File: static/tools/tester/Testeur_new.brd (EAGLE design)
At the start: 101.6 x 108 mm, 30 parts, among them IC1 MEGA8-P

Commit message: [tester] modify to V2 Alpha.
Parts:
- removed CODER-MOTOR, I²C, SV1: (no value), con-lstb:MA04-1
- removed ENCODER-SELECT, LCD-GND: (no value), con-lstb:MA05-1
- removed LCD-CONTRASTE, POTAR-CONTRASTE, RETURN, SERVO/PWM: (no value), con-lstb:MA03-1
- removed LCD-DATA: (no value), con-lstb:MA06-1
- removed LCD1-IHM, LCD2-IHM: (no value), con-lstb:MA08-1
- added AR, RETURN_IHM: (no value), pinhead:1X02
- added C1-REGULATOR1, C2-REGULATOR1: (no value), capacitor-wima:C5B5
- added IC3: (no value), v-reg:78XXS
- added JP1, JP2: (no value), pinhead:2X12
- added JP3: (no value), pinhead:1X16
- added MOTOR, X1: (no value), con-wago-500:W237-102
- added POTAR, SERVO-IHM2: (no value), con-lstb:MA03-1
- added Q2: MFR475V, transistor-power:TO220AV
- added R2: (no value), resistor:0204/7
- ALIM: device con-lstb:MA03-1 -> pinhead:1X02
- LED1, LED2: device led:LED3MM -> led:LED5MM
- R1: device rcl:0204/5 -> rcl:0204/7
- moved LED1 72.8 mm to (-3.81, -50.2), turned to 180 degrees
- moved LED2 71.8 mm to (-3.81, -43.8), turned to 180 degrees
- moved ALIM 34.4 mm to (1.91, 15.2), turned to 270 degrees
- moved IC2 27.4 mm to (-4.45, 16.5), turned to 90 degrees
- moved C1-REGULATOR 24.8 mm to (-0.64, 8.89), turned to 0 degrees
- moved C2-REGULATOR 22.8 mm to (-0.64, 24.1), turned to 0 degrees
- moved CODER-IHM 14.6 mm to (26.0, -17.8), turned to 90 degrees
- moved SERVO-IHM 14.2 mm to (44.5, -19.1), turned to 90 degrees
- moved IC1 9.44 mm to (26.0, 25.4)
- moved R3 8.64 mm to (38.1, 15.2), turned to 270 degrees
- moved R4 8.64 mm to (34.9, 15.2), turned to 270 degrees
- moved C1-CRYSTAL 8.13 mm to (26.0, 37.5), turned to 90 degrees
- moved C2-CRYSTAL 8.13 mm to (15.9, 37.5), turned to 270 degrees
- moved Q1 8.13 mm to (21.0, 37.5), turned to 270 degrees
- moved UART-IHM 6.98 mm to (15.9, -17.8), turned to 90 degrees
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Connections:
- net N$25 renamed LED1
- net N$26 renamed LED2
- removed net N$5: CODER-MOTOR.2, IC1.5
- new net 5V_POWER: C2-REGULATOR1.1, IC3.OUT, SERVO-IHM.2, SERVO-IHM2.2
- new net 5V_POW_IHM: JP2.3
- new net ALIM_EXT: C1-REGULATOR1.1, IC3.IN, MOTOR.1, X1.1
- new net ENCODER1: IC1.6, JP1.24
- new net ENCODER2: IC1.11, JP1.23
- new net GND_IHM: AR.1, C1-REGULATOR1.2, C2-REGULATOR1.2, CODER-IHM.2, ENCODER-IHM.C, ENCODER-IHM.D, I2C-IHM.2, IC3.GND, JP2.1, JP3.1, JP3.10, JP3.5, JP3.7, JP3.8, JP3.9, LED1.K, LED2.K, POTAR.3, Q2.E, RETURN_IHM.1, SERVO-IHM.1, SERVO-IHM2.1, UART-IHM.2, X1.2
- new net INT_ODO1: IC1.4, JP1.18
- new net LCD1: IC1.13, JP1.19
- new net LCD2: IC1.14, JP1.17
- new net LCD3: IC1.15, JP1.15
- new net LCD5: IC1.18, JP1.9
- new net LCD6: IC1.19, JP1.7
- new net N$25: JP2.19, JP3.4
- new net N$26: JP2.17, JP3.6
- new net N$34: JP2.7, JP3.14
- new net N$35: JP2.11, R2.1, SERVO-IHM.3
- new net N$36: JP2.8, RETURN_IHM.2
- new net N$37: AR.2, JP2.2
- new net N$39: JP3.3, POTAR.1
- new net N$40: MOTOR.2, Q2.C
- new net RETURN: IC1.26, JP1.8
- new net RX: IC1.2, JP1.14
- new net SCL: IC1.28, JP1.12
- new net SDA: IC1.27, JP1.10
- new net SELECT: IC1.12, JP1.21
- new net SENS_ODO+SERVO2: IC1.5, JP1.22
- new net SERVO/PWM: IC1.17, JP1.11
- new net TX: IC1.3, JP1.16
- new net VCC_IHM: CODER-IHM.1, I2C-IHM.1, JP2.5, JP3.2, POTAR.2, UART-IHM.1
- net GND: now also JP1.1; no longer CODER-MOTOR.4, ENCODER-SELECT.4, ENCODER-SELECT.5, I²C.2, LCD-CONTRASTE.3, LCD-GND.1, LCD-GND.2, LCD-GND.3, LCD-GND.4, LCD-GND.5, LED1.K, LED2.K, POTAR-CONTRASTE.3, RETURN.3, SERVO/PWM.3, SV1.3
- net N$10: now also I2C-IHM.3, JP2.10; no longer IC1.14, LCD-DATA.2
- net N$11: now also I2C-IHM.4, JP2.12; no longer IC1.17, SERVO/PWM.1
- net N$12: now also JP2.4, LED1.A; no longer IC1.19, LCD-DATA.6
- net N$13: now also JP2.6, LED2.A; no longer IC1.13, LCD-DATA.1
- net N$14: now also JP2.14, UART-IHM.3; no longer IC1.15, LCD-DATA.3
- net N$15: now also JP2.16, UART-IHM.4; no longer IC1.16, LCD-DATA.4
- net N$16: now also CODER-IHM.3, JP2.18; no longer IC1.18, LCD-DATA.5
- net N$17: now also CODER-IHM.4, JP2.22, SERVO-IHM2.3; no longer CODER-MOTOR.1, IC1.4
- net N$18: now also ENCODER-IHM.A, JP2.24; no longer LED2.A, R3.2
- net N$21: now also ENCODER-IHM.B, JP2.23; no longer IC1.2, SV1.1
- net N$22: now also ENCODER-IHM.E, JP2.21; no longer IC1.3, SV1.2
- net N$27: now also JP2.15, JP3.11; no longer IC1.26, RETURN.1
- net N$28: now also JP1.4; no longer LED1.A
- net N$29: now also JP2.13, JP3.12; no longer IC1.27, I²C.3
- net N$3: now also IC1.23, JP1.2; no longer LCD-CONTRASTE.1, POTAR-CONTRASTE.1
- net N$30: now also JP2.9, JP3.13; no longer IC1.28, I²C.4
- net N$6: now also ALIM.2; no longer ALIM.3
- net N$7: now also JP1.6, R3.2; no longer ENCODER-SELECT.1, IC1.6
- net N$8: now also Q2.B, R2.2; no longer ENCODER-SELECT.2, IC1.11
- net N$9: now also IC1.16, JP1.13; no longer ENCODER-SELECT.3, IC1.12
- net VCC: now also JP1.5; no longer CODER-MOTOR.3, I²C.1, LCD-CONTRASTE.2, POTAR-CONTRASTE.2, SERVO/PWM.2, SV1.4
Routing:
- net GND_IHM: track 0.00 -> 249.3 mm
- net GND: track 229.5 -> 90.8 mm, vias 2 -> 0
- net N$17: track 7.62 -> 111.0 mm
- net ENCODER1: track 0.00 -> 99.1 mm
- net VCC: track 160.4 -> 69.0 mm, vias 6 -> 0
- net SENS_ODO+SERVO2: track 0.00 -> 90.3 mm, vias 0 -> 1
- net N$21: track 9.04 -> 91.7 mm
- net ALIM_EXT: track 0.00 -> 72.6 mm
- net INT_ODO1: track 0.00 -> 71.6 mm
- net N$15: track 15.3 -> 82.8 mm
- net N$22: track 13.0 -> 77.5 mm
- net N$10: track 8.89 -> 73.0 mm
- net VCC_IHM: track 0.00 -> 64.0 mm, vias 0 -> 1
- net N$14: track 11.7 -> 75.2 mm
- net N$18: track 12.5 -> 73.7 mm
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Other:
- board text added: "A"
- board text added: "AR"
- board text added: "B"
- board text added: "GND"
- board text added: "I²C"
- board text added: "LED1"
- board text added: "LED2"
- board text added: "MOTOR"
- board text added: "POWER"
- board text added: "UART"
- board text added: "codeur"
- board text added: "encoder"
- board text added: "potar"
- board text added: "return"
- board text added: "servo"
- board text added: "servo2"

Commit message: [tester] improve V2.
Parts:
- removed UART-IHM: (no value), con-lstb:MA04-1
- added SERVO-IHM1: (no value), con-lstb:MA03-1
- added SWITCH_5V: (no value), pinhead:1X03
- moved SERVO-IHM 94.8 mm to (-50.2, -14.0)
- moved CODER-IHM 88.3 mm to (-62.2, -15.2)
- moved SERVO-IHM2 80.8 mm to (-26.0, -14.0)
- moved ALIM 79.4 mm to (-77.5, 18.4)
- moved C1-CRYSTAL 79.4 mm to (-53.3, 40.6)
- moved C1-REGULATOR 79.4 mm to (-80.0, 12.1)
- moved C1-REGULATOR1 79.4 mm to (-20.3, -47.6)
- moved C2-CRYSTAL 79.4 mm to (-63.5, 40.6)
- moved C2-REGULATOR 79.4 mm to (-80.0, 27.3)
- moved C2-REGULATOR1 79.4 mm to (-20.3, -32.4)
- moved ENCODER-IHM 79.4 mm to (-0.64, -46.4)
- moved IC1 79.4 mm to (-53.3, 28.6)
- moved IC2 79.4 mm to (-83.8, 19.7)
- moved IC3 79.4 mm to (-25.4, -40.0)
- moved JP1 79.4 mm to (-57.1, 9.53)
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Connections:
- removed net N$15: JP2.16, UART-IHM.4
- new net 5V_P/A: SERVO-IHM.2, SERVO-IHM1.2, SERVO-IHM2.2, SWITCH_5V.2
- new net N$42: JP2.16, SERVO-IHM2.3
- net 5V_POWER: now also SWITCH_5V.3; no longer SERVO-IHM.2, SERVO-IHM2.2
- net GND_IHM: now also ENCODER-IHM.B, SERVO-IHM1.1; no longer ENCODER-IHM.C, UART-IHM.2
- net N$14: now also SERVO-IHM1.3; no longer UART-IHM.3
- net N$17: no longer SERVO-IHM2.3
- net N$21: now also ENCODER-IHM.C; no longer ENCODER-IHM.B
- net VCC_IHM: now also SWITCH_5V.1; no longer UART-IHM.1
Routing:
- net N$42: track 0.00 -> 59.4 mm, vias 0 -> 2
- net N$15: track 82.8 -> 27.9 mm
- net N$38: track 0.00 -> 45.1 mm
- net 5V_P/A: track 0.00 -> 44.2 mm, vias 0 -> 1
- net GND_IHM: track 249.3 -> 291.2 mm, vias 0 -> 1
- net N$5: track 0.00 -> 33.0 mm
- net N$41: track 0.00 -> 27.9 mm
- net 5V_POWER: track 34.7 -> 9.94 mm
- net N$14: track 75.2 -> 54.7 mm, vias 0 -> 2
- net VCC_IHM: track 64.0 -> 83.4 mm, vias 1 -> 4
- net N$37: track 31.5 -> 49.7 mm
- net N$16: track 75.1 -> 90.7 mm, vias 0 -> 2
- net ALIM_EXT: track 72.6 -> 83.0 mm
- net N$17: track 111.0 -> 101.5 mm, vias 0 -> 2
- net N$45: track 0.00 -> 5.08 mm
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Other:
- board text added: "BOTTOM"
- board text added: "TOP"
- board text added: "by Fab@ENAC - 2015"
- board text added: "coder"
- board text added: "servo1"
- board text added: "servo3"
- board text removed: "UART"
- board text removed: "codeur"
- board text removed: "servo"

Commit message: [tester] add pins correspondance.
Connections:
- net RX renamed SERVO2
- net SENS_ODO+SERVO2 renamed SENS_ODO
- net TX renamed SERVO3
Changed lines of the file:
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@@
 <layer number="14" name="Route14" color="1" fill="6" visible="no" active="no"/>
 <layer number="15" name="Route15" color="4" fill="6" visible="no" active="no"/>
-<layer number="16" name="Bottom" color="1" fill="1" visible="no" active="yes"/>
+<layer number="16" name="Bottom" color="1" fill="1" visible="yes" active="yes"/>
 <layer number="17" name="Pads" color="2" fill="1" visible="yes" active="yes"/>
 <layer number="18" name="Vias" color="2" fill="1" visible="yes" active="yes"/>
 <layer number="19" name="Unrouted" color="6" fill="1" visible="yes" active="yes"/>
 <layer number="20" name="Dimension" color="15" fill="1" visible="yes" active="yes"/>
-<layer number="21" name="tPlace" color="7" fill="1" visible="no" active="yes"/>
-<layer number="22" name="bPlace" color="7" fill="1" visible="no" active="yes"/>
-<layer number="23" name="tOrigins" color="15" fill="1" visible="no" active="yes"/>
-<layer number="24" name="bOrigins" color="15" fill="1" visible="no" active="yes"/>
-<layer number="25" name="tNames" color="7" fill="1" visible="no" active="yes"/>
-<layer number="26" name="bNames" color="7" fill="1" visible="no" active="yes"/>
-<layer number="27" name="tValues" color="7" fill="1" visible="no" active="yes"/>
-<layer number="28" name="bValues" color="7" fill="1" visible="no" active="yes"/>
-<layer number="29" name="tStop" color="7" fill="3" visible="no" active="yes"/>
-<layer number="30" name="bStop" color="7" fill="6" visible="no" active="yes"/>
-<layer number="31" name="tCream" color="7" fill="4" visible="no" active="yes"/>
-<layer number="32" name="bCream" color="7" fill="5" visible="no" active="yes"/>
-<layer number="33" name="tFinish" color="6" fill="3" visible="no" active="yes"/>
-<layer number="34" name="bFinish" color="6" fill="6" visible="no" active="yes"/>
-<layer number="35" name="tGlue" color="7" fill="4" visible="no" active="yes"/>
-<layer number="36" name="bGlue" color="7" fill="5" visible="no" active="yes"/>
-<layer number="37" name="tTest" color="7" fill="1" visible="no" active="yes"/>
-<layer number="38" name="bTest" color="7" fill="1" visible="no" active="yes"/>
-<layer number="39" name="tKeepout" color="4" fill="11" visible="no" active="yes"/>
-<layer number="40" name="bKeepout" color="1" fill="11" visible="no" active="yes"/>
-<layer number="41" name="tRestrict" color="4" fill="10" visible="no" active="yes"/>
-<layer number="42" name="bRestrict" color="1" fill="10" visible="no" active="yes"/>
-<layer number="43" name="vRestrict" color="2" fill="10" visible="no" active="yes"/>
-<layer number="44" name="Drills" color="7" fill="1" visible="no" active="yes"/>
-<layer number="45" name="Holes" color="7" fill="1" visible="no" active="yes"/>
-<layer number="46" name="Milling" color="3" fill="1" visible="no" active="yes"/>
-<layer number="47" name="Measures" color="7" fill="1" visible="no" active="yes"/>
-<layer number="48" name="Document" color="7" fill="1" visible="no" active="yes"/>
-<layer number="49" name="Reference" color="7" fill="1" visible="no" active="yes"/>
-<layer number="51" name="tDocu" color="7" fill="1" visible="no" active="yes"/>
-<layer number="52" name="bDocu" color="7" fill="1" visible="no" active="yes"/>
+<layer number="21" name="tPlace" color="7" fill="1" visible="yes" active="yes"/>
+<layer number="22" name="bPlace" color="7" fill="1" visible="yes" active="yes"/>
+<layer number="23" name="tOrigins" color="15" fill="1" visible="yes" active="yes"/>
+<layer number="24" name="bOrigins" color="15" fill="1" visible="yes" active="yes"/>
+<layer number="25" name="tNames" color="7" fill="1" visible="yes" active="yes"/>
+<layer number="26" name="bNames" color="7" fill="1" visible="yes" active="yes"/>
+<layer number="27" name="tValues" color="7" fill="1" visible="yes" active="yes"/>
+<layer number="28" name="bValues" color="7" fill="1" visible="yes" active="yes"/>
+<layer number="29" name="tStop" color="7" fill="3" visible="yes" active="yes"/>
+<layer number="30" name="bStop" color="7" fill="6" visible="yes" active="yes"/>
+<layer number="31" name="tCream" color="7" fill="4" visible="yes" active="yes"/>
+<layer number="32" name="bCream" color="7" fill="5" visible="yes" active="yes"/>
+<layer number="33" name="tFinish" color="6" fill="3" visible="yes" active="yes"/>
+<layer number="34" name="bFinish" color="6" fill="6" visible="yes" active="yes"/>
+<layer number="35" name="tGlue" color="7" fill="4" visible="yes" active="yes"/>
+<layer number="36" name="bGlue" color="7" fill="5" visible="yes" active="yes"/>
+<layer number="37" name="tTest" color="7" fill="1" visible="yes" active="yes"/>
+<layer number="38" name="bTest" color="7" fill="1" visible="yes" active="yes"/>
+<layer number="39" name="tKeepout" color="4" fill="11" visible="yes" active="yes"/>
+<layer number="40" name="bKeepout" color="1" fill="11" visible="yes" active="yes"/>
+<layer number="41" name="tRestrict" color="4" fill="10" visible="yes" active="yes"/>
+<layer number="42" name="bRestrict" color="1" fill="10" visible="yes" active="yes"/>
+<layer number="43" name="vRestrict" color="2" fill="10" visible="yes" active="yes"/>
+<layer number="44" name="Drills" color="7" fill="1" visible="yes" active="yes"/>
+<layer number="45" name="Holes" color="7" fill="1" visible="yes" active="yes"/>
+<layer number="46" name="Milling" color="3" fill="1" visible="yes" active="yes"/>
+<layer number="47" name="Measures" color="7" fill="1" visible="yes" active="yes"/>
+<layer number="48" name="Document" color="7" fill="1" visible="yes" active="yes"/>
+<layer number="49" name="Reference" color="7" fill="1" visible="yes" active="yes"/>
+<layer number="51" name="tDocu" color="7" fill="1" visible="yes" active="yes"/>
+<layer number="52" name="bDocu" color="7" fill="1" visible="yes" active="yes"/>
 <layer number="91" name="Nets" color="2" fill="1" visible="no" active="no"/>
 <layer number="92" name="Busses" color="1" fill="1" visible="no" active="no"/>
@@
 <wire x1="-63.5" y1="15.24" x2="-63.5" y2="10.795" width="0.8128" layer="16"/>
 </signal>
-<signal name="SENS_ODO+SERVO2">
+<signal name="SENS_ODO">
 <contactref element="IC1" pad="5"/>
 <contactref element="JP1" pad="22"/>
@@
 <via x="-89.535" y="-56.515" extent="1-16" drill="3.2"/>
 </signal>
-<signal name="TX">
+<signal name="SERVO3">
 <contactref element="IC1" pad="3"/>
 <wire x1="-55.245" y1="2.54" x2="-39.37" y2="2.54" width="0.8128" layer="16"/>
@@
 <wire x1="-55.245" y1="2.54" x2="-60.96" y2="8.255" width="0.8128" layer="16"/>
 </signal>
-<signal name="RX">
+<signal name="SERVO2">
 <contactref element="IC1" pad="2"/>
 <wire x1="-53.975" y1="3.81" x2="-40.005" y2="3.81" width="0.8128" layer="1"/>

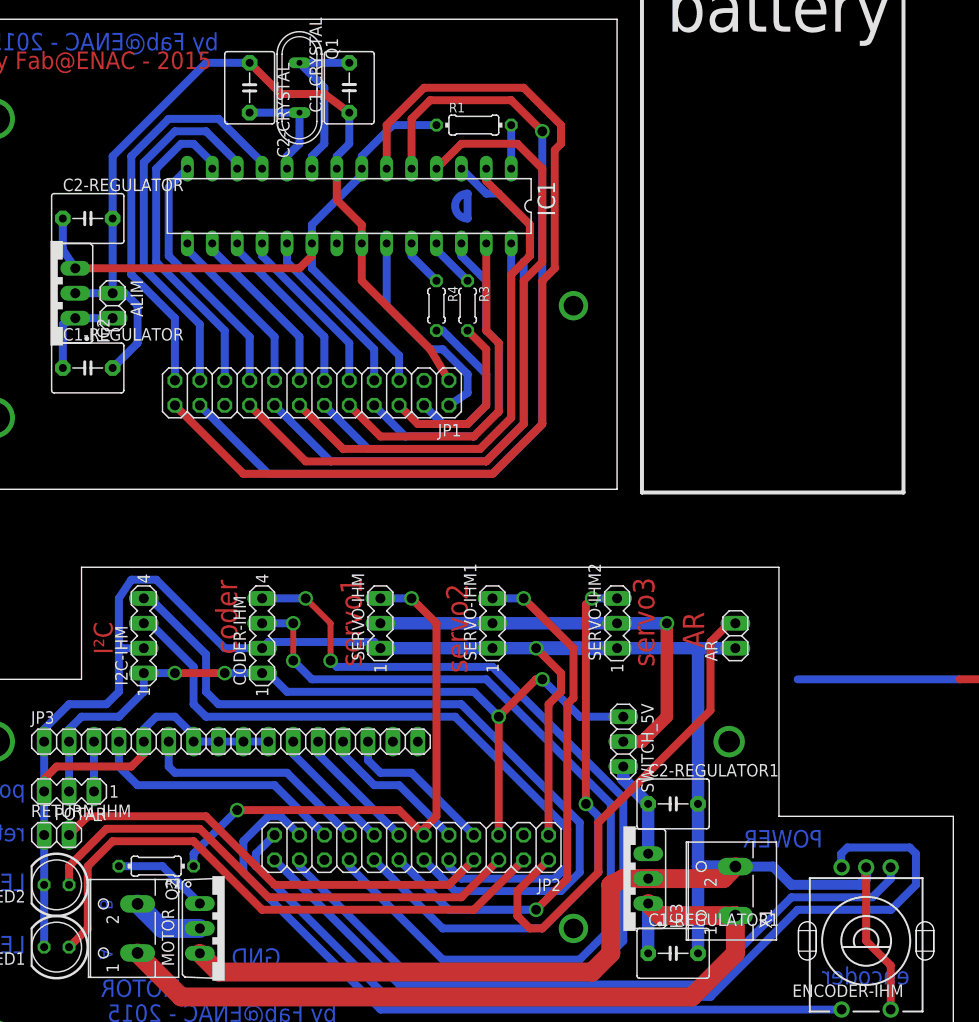
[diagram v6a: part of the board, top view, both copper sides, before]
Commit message: [tester] add "pont diviseur" and some modification.
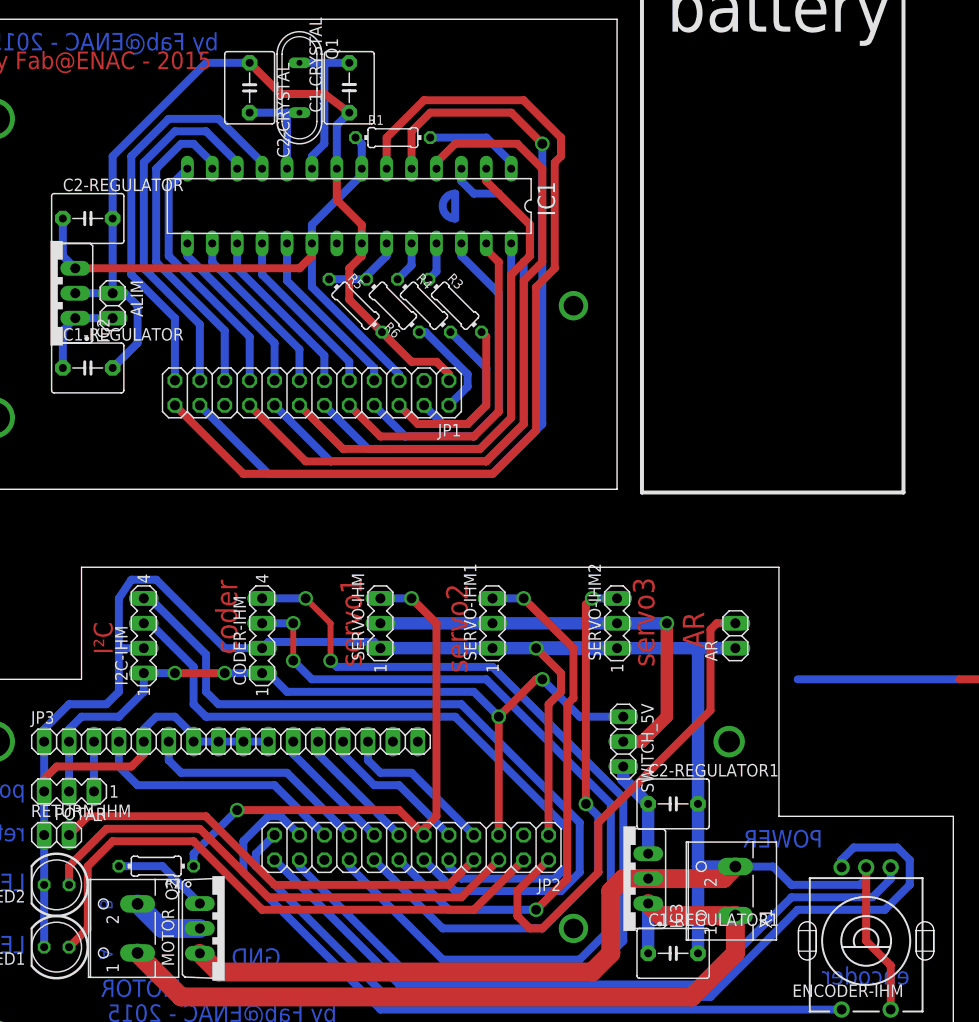
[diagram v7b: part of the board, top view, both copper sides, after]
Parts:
- added R5, R6: (no value), rcl:0204/7
- R3, R4: device resistor:0204/5 -> resistor:0204/7
- moved R1 8.35 mm to (-48.9, 35.6)
- moved R3 1.27 mm to (-42.5, 18.4), turned to 315 degrees
- moved R4 1.27 mm to (-45.7, 18.4), turned to 315 degrees
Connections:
- new net N$46: IC1.23, R5.1, R6.2
- net GND: now also R5.2
- net N$3: now also R6.1; no longer IC1.23
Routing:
- net N$3: track 21.7 -> 10.7 mm
- net N$46: track 0.00 -> 8.32 mm
- net VCC: track 69.0 -> 62.3 mm
- net N$4: track 4.45 -> 9.94 mm
- net GND: track 90.6 -> 93.4 mm
- net SENS_ODO: track 90.3 -> 87.7 mm
- net ENCODER1: track 99.1 -> 96.6 mm
- net N$21: track 94.3 -> 92.2 mm
- net LED2: track 5.13 -> 3.98 mm
- net N$28: track 18.0 -> 16.9 mm
- net N$1: track 17.5 -> 16.4 mm
- net SERVO3: track 59.3 -> 60.0 mm
- net N$37: track 49.7 -> 50.5 mm
- net LED1: track 4.86 -> 4.25 mm
- net N$2: track 11.3 -> 10.8 mm
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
